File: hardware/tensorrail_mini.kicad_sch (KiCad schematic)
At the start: 63 parts, among them J1 USB4135-GF-A, J2 JTAG_ARM_10P, J3 EXP_40P_2x20, SW1 RESET, SW2 PROG/BOOT, U1 TPS62130ARGTR, U2 TPS62130ARGTR, U3 INA219AIDCNT, U4 W25Q128JVxIM, U5 SG-8002CA-50MHz

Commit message: Fix KiCad schematic for viewer import
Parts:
- removed C1, C16, C3, C7: 10uF/10V, Capacitor_SMD:C_0805_2012Metric, symbol Device:C
- removed C10, C11, C12, C13, C15, C17, C18, C2, C4, C6, C8: 100nF/25V, Capacitor_SMD:C_0402_1005Metric, symbol Device:C
- removed C14: 1uF/25V, Capacitor_SMD:C_0402_1005Metric, symbol Device:C
- removed C5, C9: 100uF/6.3V, Capacitor_SMD:C_1210_3225Metric, symbol Device:C
- removed D1: PMEG4010CEJ, Diode_SMD:D_SOD-123, symbol Device:D_Schottky
- removed D2: LED_PWR, LED_SMD:LED_0402_1005Metric, symbol Device:LED
- removed D3: LED_BUSY, LED_SMD:LED_0402_1005Metric, symbol Device:LED
- removed D4: LED_DONE, LED_SMD:LED_0402_1005Metric, symbol Device:LED
- removed D5: LED_HB, LED_SMD:LED_0402_1005Metric, symbol Device:LED
- removed J1: USB4135-GF-A, Connector_USB:GCT_USB4135-GF-A_Horizontal, symbol Connector_USB:USB_C_Receptacle_USB2.0
- removed J2: JTAG_ARM_10P, Connector_IDC:IDC_Header_2x05_P1.27mm_Vertical, symbol Connector_IDC:IDC_Header_2x05_P1.27mm_Vertical
- removed J3: EXP_40P_2x20, Connector_PinHeader_2.54mm:PinHeader_2x20_P2.54mm_Vertical, symbol Connector_PinHeader_2.54mm:PinHeader_2x20_P2.54mm_Vertical
- removed L1: 2.2uH/3A, Inductor_SMD:L_Bourns_SRR4011, symbol Device:L
- removed L2: 1.5uH/3A, Inductor_SMD:L_Bourns_SRR4011, symbol Device:L
- removed R1, R2: 5.1k, Resistor_SMD:R_0402_1005Metric, symbol Device:R
- removed R10, R11, R18, R19: 10k, Resistor_SMD:R_0402_1005Metric, symbol Device:R
- removed R12, R13, R14: 100R, Resistor_SMD:R_0402_1005Metric, symbol Device:R
- removed R15, R16, R17: 4.7k, Resistor_SMD:R_0402_1005Metric, symbol Device:R
- removed R20, R21, R22, R23: 1k, Resistor_SMD:R_0402_1005Metric, symbol Device:R
- removed R3: 464k, Resistor_SMD:R_0402_1005Metric, symbol Device:R
- removed R4, R6: 100k, Resistor_SMD:R_0402_1005Metric, symbol Device:R
- removed R5: 103k, Resistor_SMD:R_0402_1005Metric, symbol Device:R
- removed R7: 0R1/1W, Resistor_SMD:R_2512_6332Metric, symbol Device:R
- removed SW1: RESET, Button_Switch_SMD:SW_SPST_TL3342, symbol Switch:SW_Push
- removed SW2: PROG/BOOT, Button_Switch_SMD:SW_SPST_TL3342, symbol Switch:SW_Push
- removed TP1: +5V, TestPoint:TestPoint_Pad_D1.5mm, symbol TestPoint:TestPoint_Pad_D1.5mm
- removed TP2: +3V3, TestPoint:TestPoint_Pad_D1.5mm, symbol TestPoint:TestPoint_Pad_D1.5mm
- removed TP3: +1V2, TestPoint:TestPoint_Pad_D1.5mm, symbol TestPoint:TestPoint_Pad_D1.5mm
- removed TP4: GND, TestPoint:TestPoint_Pad_D1.5mm, symbol TestPoint:TestPoint_Pad_D1.5mm
- removed TP5: SCL, TestPoint:TestPoint_Pad_D1.5mm, symbol TestPoint:TestPoint_Pad_D1.5mm
- removed TP6: SDA, TestPoint:TestPoint_Pad_D1.5mm, symbol TestPoint:TestPoint_Pad_D1.5mm
- removed TP7: CLK_50M, TestPoint:TestPoint_Pad_D1.5mm, symbol TestPoint:TestPoint_Pad_D1.5mm
- removed U1, U2: TPS62130ARGTR, Package_TO_SOT_SMD:SOT-23-8, symbol Regulator_Switching:TPS62130
- removed U3: INA219AIDCNT, Package_TO_SOT_SMD:SOT-23-8, symbol Sensor_Current:INA219xIDCNT
- removed U4: W25Q128JVxIM, Package_SO:SOIC-8_3.9x4.9mm_P1.27mm, symbol Memory_Flash:W25Q128JVxIM
- removed U5: SG-8002CA-50MHz, Oscillator:Oscillator_SMD_Epson_SG-8002CA-4Pin_3.2x2.5mm, symbol Oscillator:SG-8002CA
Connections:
- no-connect marks 4 -> 0
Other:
- note added: "+3V3 and GND"
- note added: "+5V, +3V3, +1V2"
- note added: "2.2uH inductor"
- note added: "20mOhm shunt"
- note added: "2x5 1.27mm"
- note added: "3.3V system rail"
- note added: "464k/100k feedback"
- note added: "649k/100k feedback"
- note added: "CC1/CC2: 5.1k Rd"
- note added: "CLK_50M"
- note added: "CLK_50M into ECP5"
- note added: "CS, WP#, HOLD# pull-ups"
- note added: "D2 power"
- note added: "D3 busy"
- note added: "D4 done"
- note added: "D5 heartbeat"
- note added: "Engineering Notes"
- note added: "FPGA core rail"
- note added: "GND, SCL, SDA"
- note added: "GPIO / UART / I2C"
- note added: "I2C telemetry"
- note added: "INA219xIDCNT"
- note added: "INT8 systolic-array fabric"
- note added: "J1 USB-C POWER INPUT"
- note added: "J2 JTAG HEADER"
- note added: "J3 40-PIN EXPANSION"
- note added: "JTAG programming"
- note added: "KiCad viewer-valid architecture schematic: USB-C power, monitored rails, FPGA module IO, SPI boot flash, oscillator, JTAG, expansion, status controls."
- note added: "MOD1 LATTICE ECP5 MODULE"
- note added: "OrangeCrab 85F compatible"
- note added: "PSRAM lanes"
- note added: "Power tree is separated into +3V3 IO and +1V2 core rails with INA219 current telemetry on the core path."
- note added: "RESET_N"
- note added: "SG-8002CA class XO"
- note added: "SPI breakout"
- note added: "SPI_SCK / MOSI / MISO"
- note added: "SW1 reset"
- note added: "SW2 boot/program"
- note added: "TCK/TMS/TDI/TDO"
- note added: "TEST POINTS"
- note added: "TPS62130ARGTR"
- note added: "TensorRail-Mini ECP5 INT8 AI Accelerator Carrier"
- note added: "The ECP5 module hosts the RTL accelerator; board resources expose boot, programming, IO, and measurement hooks."
- note added: "This sheet is a clean KiCad-compatible architecture schematic for repository import and viewer validation."
- note added: "U1 3.3V BUCK"
- note added: "U2 1.2V CORE BUCK"
- note added: "U3 POWER MONITOR"
- note added: "U4 SPI FLASH"
- note added: "U5 50 MHz OSCILLATOR"
- note added: "UART + SPI boot"
- note added: "USB4135-GF-A"
- note added: "USER IO"
- note added: "VBUS protection + bulk/HF bypass"
- note added: "VCORE_SENSED"
- note added: "W25Q128JV"
- note added: "future sensor IO"
- note added: "local 100nF bypass"
- title: TensorRail-Mini — ECP5 AI Accelerator Carrier Board -> TensorRail-Mini ECP5 INT8 AI Accelerator Carrier

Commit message: Replace viewer design artifacts with clean layouts
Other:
- note added: "1.2V BUCK"
- note added: "3.3V BUCK"
- note added: "3V3/GND"
- note added: "40-PIN EXPANSION"
- note added: "50MHz XO"
- note added: "5V VBUS"
- note added: "CC pull-downs"
- note added: "ECP5 MODULE"
- note added: "GPIO bus"
- note added: "I2C"
- note added: "INA219"
- note added: "INT8 systolic RTL"
- note added: "IO rail"
- note added: "JTAG"
- note added: "OrangeCrab 85F"
- note added: "PCB + BOM"
- note added: "REPO PROOF"
- note added: "RTL + sim"
- note added: "SPI FLASH"
- note added: "TCK/TMS"
- note added: "TDI/TDO"
- note added: "TPS62130"
- note added: "TensorRail-Mini ECP5 INT8 Accelerator Carrier"
- note added: "UART/I2C/SPI"
- note added: "UART/PSRAM IO"
- note added: "USB-C INPUT"
- note added: "Viewer-focused KiCad schematic: power, FPGA module, boot, clock, programming, IO, validation."
- note added: "boot image"
- note added: "busy/done"
- note added: "clock source"
- note added: "clock/reset"
- note added: "core current"
- note added: "core rail"
- note added: "flash/header"
- note added: "heartbeat"
- note added: "local bypass"
- note added: "ngspice + Python"
- note added: "protection"
- note added: "rails"
- note added: "reset/boot"
- note added: "sense shunt"
- note removed: "+3V3 and GND"
- note removed: "+5V, +3V3, +1V2"
- note removed: "2.2uH inductor"
- note removed: "20mOhm shunt"
- note removed: "2x5 1.27mm"
- note removed: "3.3V system rail"
- note removed: "464k/100k feedback"
- note removed: "649k/100k feedback"
- note removed: "CC1/CC2: 5.1k Rd"
- note removed: "CLK_50M"
- note removed: "CLK_50M into ECP5"
- note removed: "CS, WP#, HOLD# pull-ups"
- note removed: "D2 power"
- note removed: "D3 busy"
- note removed: "D4 done"
- note removed: "D5 heartbeat"
- note removed: "Engineering Notes"
- note removed: "FPGA core rail"
- note removed: "GND, SCL, SDA"
- note removed: "GPIO / UART / I2C"
- note removed: "INA219xIDCNT"
- note removed: "INT8 systolic-array fabric"
- note removed: "J1 USB-C POWER INPUT"
- note removed: "J2 JTAG HEADER"
- note removed: "J3 40-PIN EXPANSION"
- note removed: "JTAG programming"
- note removed: "KiCad viewer-valid architecture schematic: USB-C power, monitored rails, FPGA module IO, SPI boot flash, oscillator, JTAG, expansion, status controls."
- note removed: "MOD1 LATTICE ECP5 MODULE"
- note removed: "OrangeCrab 85F compatible"
- note removed: "PSRAM lanes"
- note removed: "Power tree is separated into +3V3 IO and +1V2 core rails with INA219 current telemetry on the core path."
- note removed: "RESET_N"
- note removed: "SG-8002CA class XO"
- note removed: "SPI breakout"
- note removed: "SPI_SCK / MOSI / MISO"
- note removed: "SW1 reset"
- note removed: "SW2 boot/program"
- note removed: "TCK/TMS/TDI/TDO"
- note removed: "TPS62130ARGTR"
- note removed: "TensorRail-Mini ECP5 INT8 AI Accelerator Carrier"
- note removed: "The ECP5 module hosts the RTL accelerator; board resources expose boot, programming, IO, and measurement hooks."
- note removed: "This sheet is a clean KiCad-compatible architecture schematic for repository import and viewer validation."
- note removed: "U1 3.3V BUCK"
- note removed: "U2 1.2V CORE BUCK"
- note removed: "U3 POWER MONITOR"
- note removed: "U4 SPI FLASH"
- note removed: "U5 50 MHz OSCILLATOR"
- note removed: "UART + SPI boot"
- note removed: "USB4135-GF-A"
- note removed: "VBUS protection + bulk/HF bypass"
- note removed: "VCORE_SENSED"
- note removed: "future sensor IO"
- note removed: "local 100nF bypass"
- title: TensorRail-Mini ECP5 INT8 AI Accelerator Carrier -> TensorRail-Mini ECP5 INT8 Accelerator Carrier

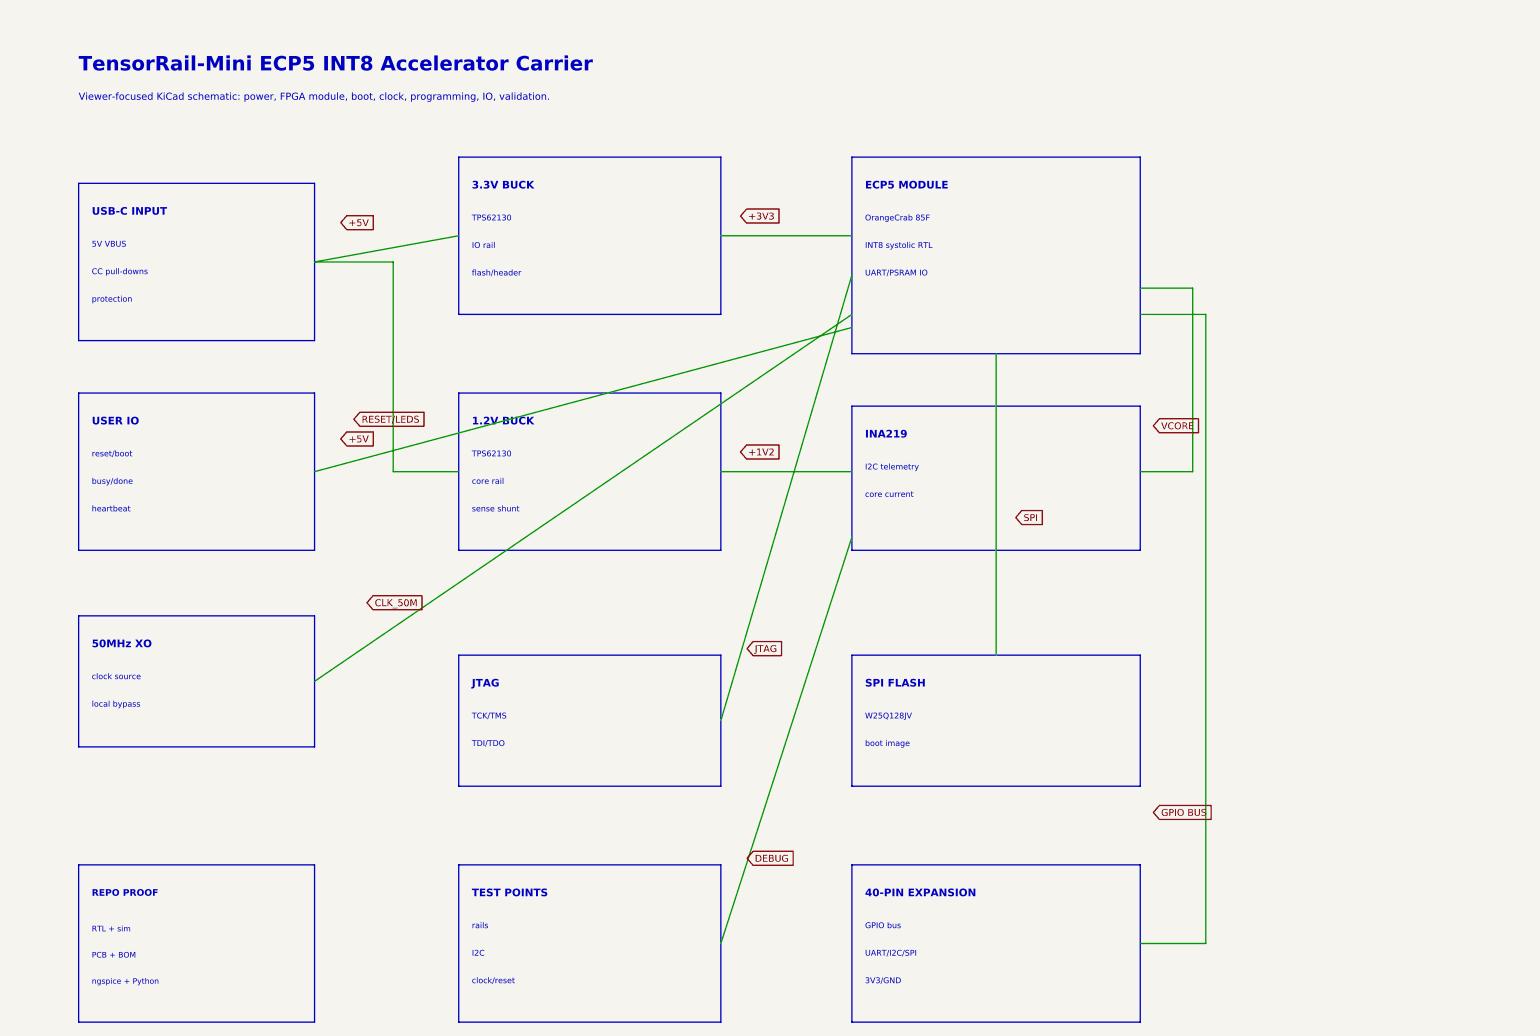
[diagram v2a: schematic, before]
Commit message: Make KiCad viewer artifacts readable
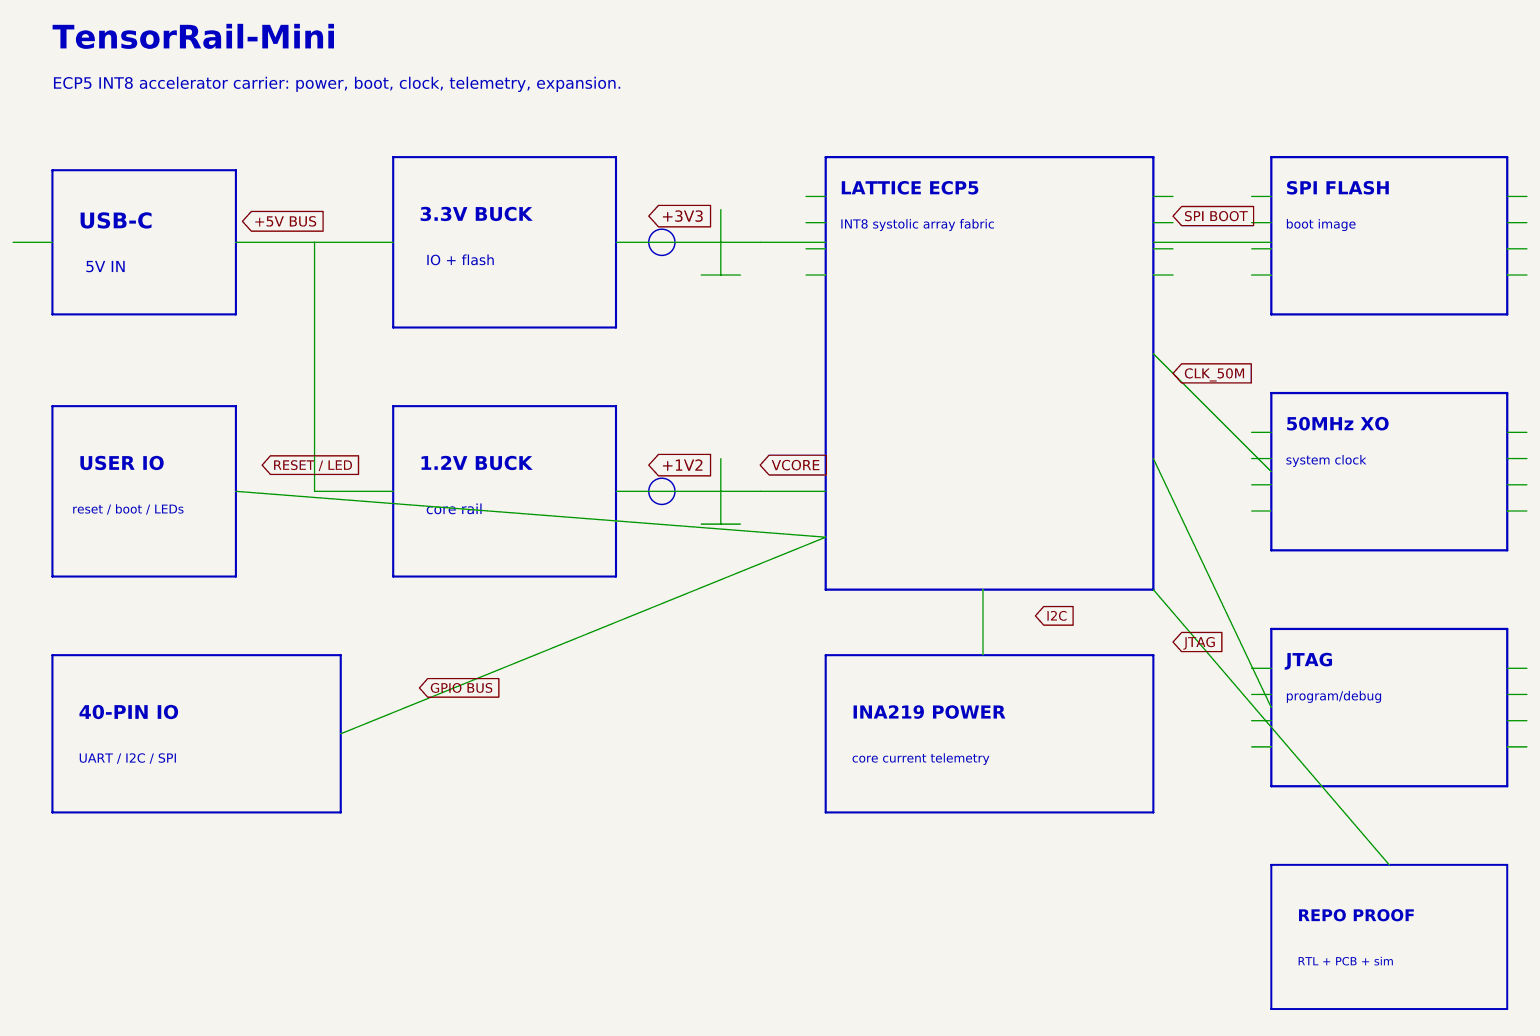
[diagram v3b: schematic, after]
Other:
- note added: "40-PIN IO"
- note added: "5V IN"
- note added: "ECP5 INT8 accelerator carrier: power, boot, clock, telemetry, expansion."
- note added: "INA219 POWER"
- note added: "INT8 systolic array fabric"
- note added: "IO + flash"
- note added: "LATTICE ECP5"
- note added: "RTL + PCB + sim"
- note added: "TensorRail-Mini"
- note added: "UART / I2C / SPI"
- note added: "USB-C"
- note added: "core current telemetry"
- note added: "program/debug"
- note added: "reset / boot / LEDs"
- note added: "system clock"
- note removed: "3V3/GND"
- note removed: "40-PIN EXPANSION"
- note removed: "5V VBUS"
- note removed: "CC pull-downs"
- note removed: "ECP5 MODULE"
- note removed: "GPIO bus"
- note removed: "I2C"
- note removed: "I2C telemetry"
- note removed: "INA219"
- note removed: "INT8 systolic RTL"
- note removed: "IO rail"
- note removed: "OrangeCrab 85F"
- note removed: "PCB + BOM"
- note removed: "RTL + sim"
- note removed: "TCK/TMS"
- note removed: "TDI/TDO"
- note removed: "TEST POINTS"
- note removed: "TPS62130"
- note removed: "TensorRail-Mini ECP5 INT8 Accelerator Carrier"
- note removed: "UART/I2C/SPI"
- note removed: "UART/PSRAM IO"
- note removed: "USB-C INPUT"
- note removed: "Viewer-focused KiCad schematic: power, FPGA module, boot, clock, programming, IO, validation."
- note removed: "W25Q128JV"
- note removed: "busy/done"
- note removed: "clock source"
- note removed: "clock/reset"
- note removed: "core current"
- note removed: "flash/header"
- note removed: "heartbeat"
- note removed: "local bypass"
- note removed: "ngspice + Python"
- note removed: "protection"
- note removed: "rails"
- note removed: "reset/boot"
- note removed: "sense shunt"
